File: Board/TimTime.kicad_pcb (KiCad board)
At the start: 4 copper layers, 1.2 x 12 mm, 57 parts, among them IC1 MCP73834-CNI_MF, IC2 LT1761ES5-2.8#TRMPBF, J1 USB4085-GF-A_REVA, J2 SJ1-3523NG, J3 Conn_01x04, J4 Conn_01x06, J5 Conn_01x02, J6 Conn_01x02, U1 STM32L433CCTx, U2 24AA00T_OT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

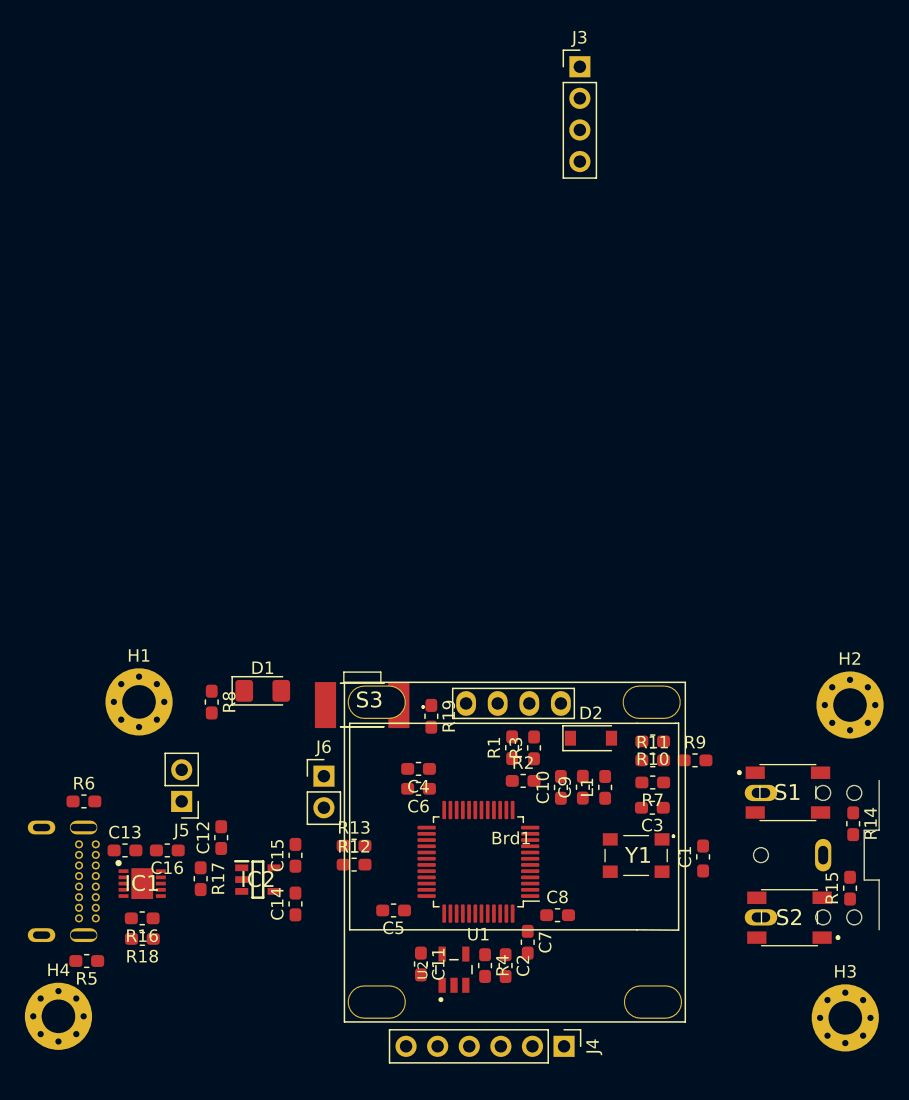
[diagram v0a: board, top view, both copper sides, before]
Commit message: Layout/Routing
Full V01 layout and routing
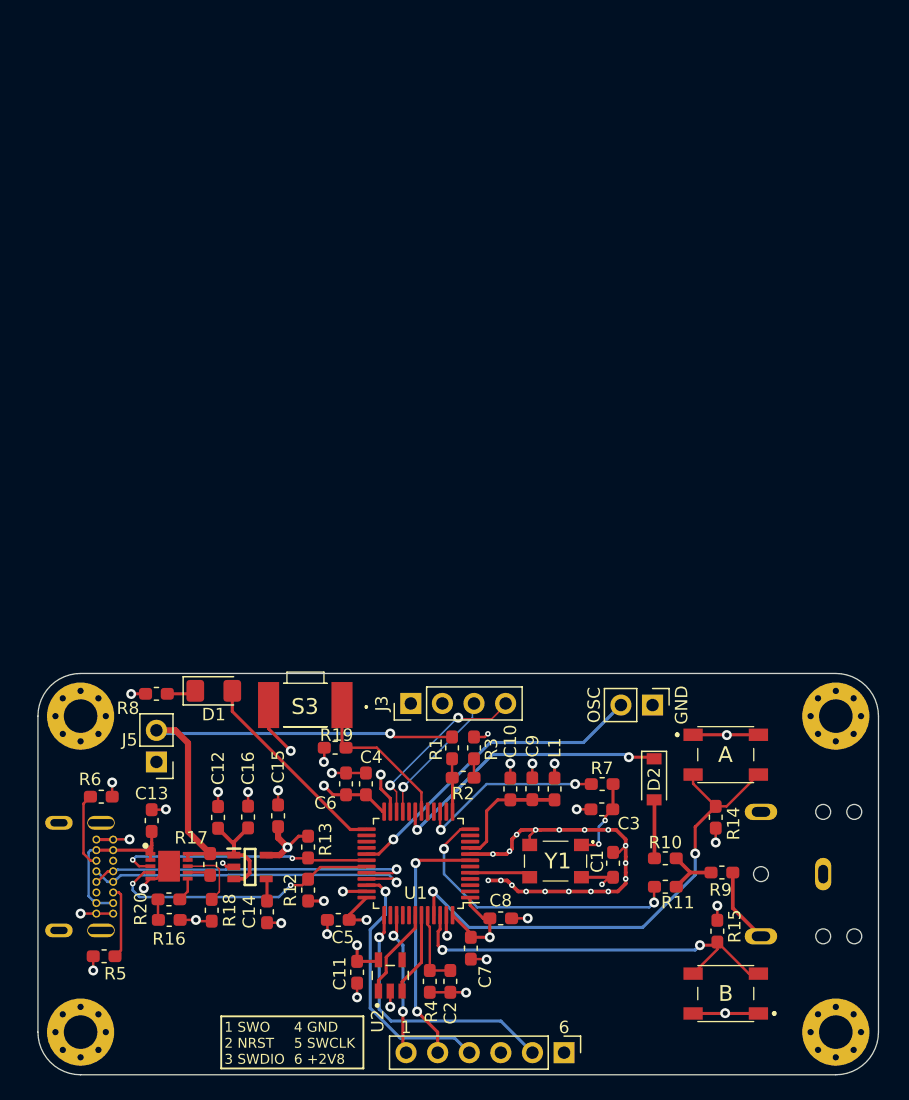
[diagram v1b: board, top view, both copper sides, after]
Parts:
- removed Brd1: SSD1306, SSD1306:128x64OLED
- added G***: LOGO, Slate_Logo:Slate_Logo_01_Back_Silk, F.Cu at (143.0, 104.4)
- added R20: 2K, Resistor_SMD:R_0603_1608Metric_Pad1.05x0.95mm_HandSolder, F.Cu at (120.9, 109.0)
- moved J3 53.0 mm to (140.3, 91.6), turned to 90 degrees
- moved GND 27.0 mm to (159.8, 91.7), turned to 270 degrees
- moved R15 11.2 mm to (165.0, 109.9)
- moved R14 11.1 mm to (164.8, 100.7)
- moved R11 10.2 mm to (160.8, 106.3)
- moved R10 9.45 mm to (160.8, 104.0)
- moved R9 9.27 mm to (165.3, 105.2)
- moved R19 8.14 mm to (134.3, 95.1), turned to 180 degrees
- moved B 7.96 mm to (165.7, 114.9)
- moved C1 7.26 mm to (156.6, 104.4)
- moved C16 7.02 mm to (127.3, 100.7), turned to 90 degrees
- moved Y1 6.49 mm to (152.0, 104.2)
- moved D2 6.06 mm to (159.9, 97.7), turned to 270 degrees
- moved R18 6.03 mm to (124.3, 108.2), turned to 270 degrees
- moved A 5.85 mm to (165.7, 95.7)
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- renumbered S1 to A, S2 to B, J6 to GND
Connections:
- R16 pad 2: GND -> Net-(R16-Pad2)
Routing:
- net GND: track 0.00 -> 79.9 mm, vias 0 -> 48
- net +BATT: track 0.00 -> 50.3 mm, vias 0 -> 1
- net +2V8: track 0.00 -> 49.2 mm, vias 0 -> 11
- net BTN_A: track 0.00 -> 40.2 mm, vias 0 -> 2
- net BTN_B: track 0.00 -> 33.1 mm, vias 0 -> 2
- net USB_D+: track 0.00 -> 27.5 mm, vias 0 -> 1
- net USB_D-: track 0.00 -> 27.1 mm, vias 0 -> 1
- net OSC: track 0.00 -> 25.4 mm, vias 0 -> 1
- net TC_IN: track 0.00 -> 24.4 mm, vias 0 -> 2
- net TC_OUT: track 0.00 -> 23.2 mm, vias 0 -> 2
- net STAT2: track 0.00 -> 22.4 mm, vias 0 -> 2
- net SWCLK: track 0.00 -> 21.5 mm, vias 0 -> 1
- net SWDIO: track 0.00 -> 21.1 mm, vias 0 -> 1
- net STAT1: track 0.00 -> 20.7 mm, vias 0 -> 2
- net NRST: track 0.00 -> 20.5 mm, vias 0 -> 2
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- added copper zone on In2.Cu, net +2V8
- added copper zone on In1.Cu, net GND
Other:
- board size 1.2 x 12 mm -> 67.6 x 32.3 mm
- board text added: "+BATT"
- board text added: "1"
- board text added: "1 SWO 2 NRST 3 SWDIO"
- board text added: "4 GND 5 SWCLK 6 +2V8"
- board text added: "6"
- board text added: "GND"
- board text added: "OSC"

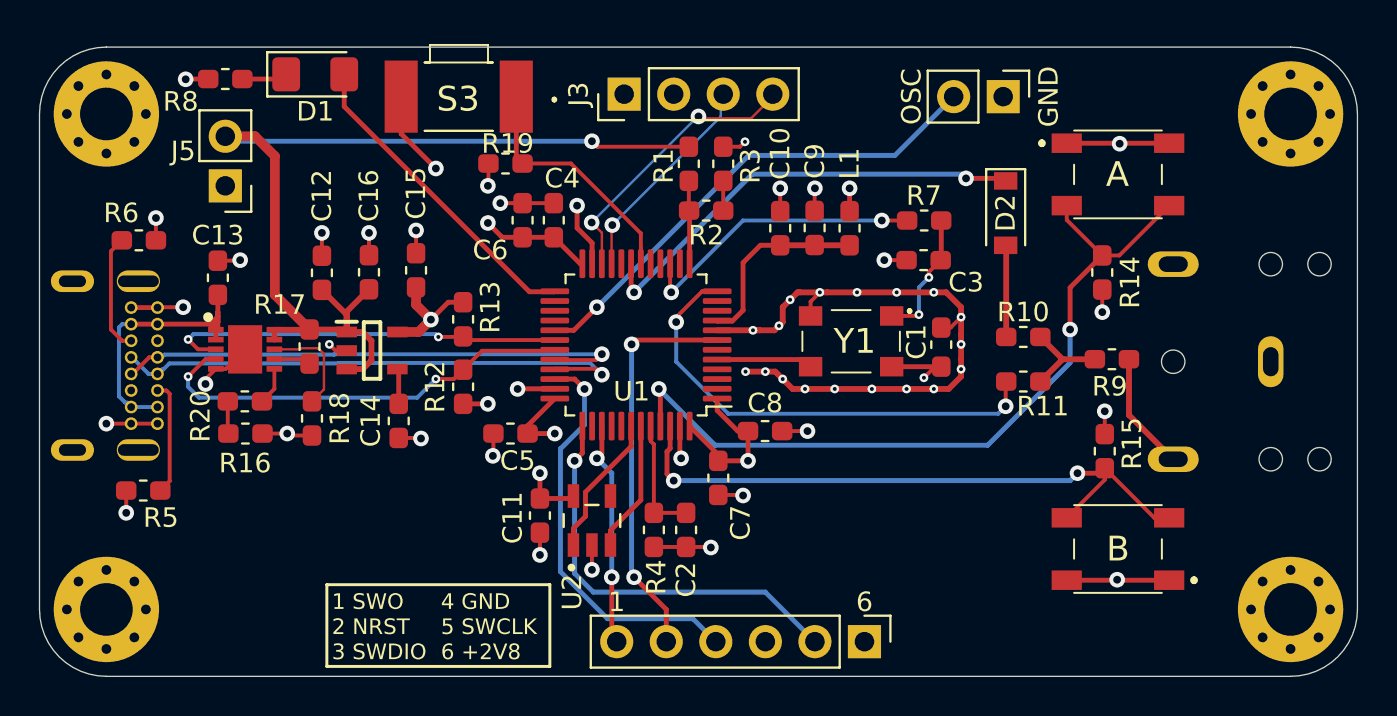
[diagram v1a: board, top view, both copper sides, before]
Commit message: Update layout
Smaller footprint
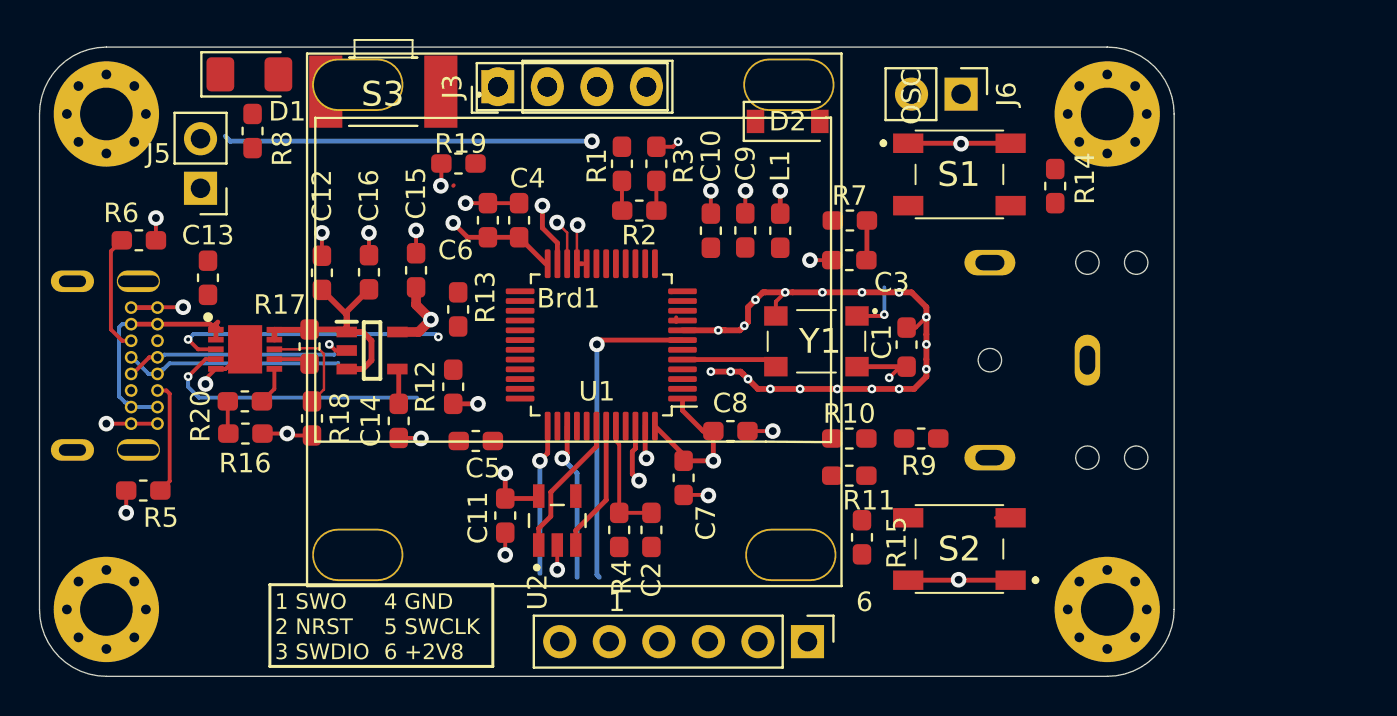
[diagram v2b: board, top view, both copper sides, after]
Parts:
- removed G***: LOGO, Slate_Logo:Slate_Logo_01_Back_Silk
- added Brd1: SSD1306, SSD1306:128x64OLED, F.Cu at (137.5, 101.8)
- moved R15 13.2 mm to (152.5, 114.3), turned to 270 degrees
- moved D2 12.1 mm to (148.7, 93.0), turned to 0 degrees
- moved R9 10.6 mm to (155.6, 109.2)
- moved R10 10.3 mm to (151.9, 109.2)
- moved R11 10.1 mm to (151.9, 111.1)
- moved J2 9.40 mm to (164.1, 105.2)
- moved H2 9.40 mm to (165.1, 92.6)
- moved H3 9.40 mm to (165.1, 118.0)
- moved S1 8.13 mm to (157.5, 95.7)
- moved S2 8.13 mm to (157.5, 114.9)
- moved J3 6.49 mm to (133.9, 91.2)
- moved R14 5.05 mm to (162.4, 96.3), turned to 90 degrees
- moved S3 3.88 mm to (128.0, 91.4)
- moved C3 3.81 mm to (151.9, 100.1)
- moved R7 3.81 mm to (151.9, 98.0)
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- renumbered GND to J6, A to S1, B to S2
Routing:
- net BTN_A: track 40.2 -> 0.00 mm, vias 2 -> 0
- net BTN_B: track 33.1 -> 3.76 mm, vias 2 -> 1
- net OSC: track 25.4 -> 0.00 mm, vias 1 -> 0
- net TC_IN: track 24.4 -> 0.08 mm, vias 2 -> 0
- net TC_OUT: track 23.2 -> 0.00 mm, vias 2 -> 0
- net SWDIO: track 21.1 -> 0.00 mm, vias 1 -> 0
- net +BATT: track 50.3 -> 32.6 mm
- net LED_STATUS: track 16.4 -> 0.00 mm
- net USB_D+: track 27.5 -> 11.2 mm, vias 1 -> 0
- net USB_D-: track 27.1 -> 10.9 mm, vias 1 -> 0
- net TCVC: track 15.1 -> 0.00 mm, vias 2 -> 0
- net SWCLK: track 21.5 -> 7.71 mm
- net BTN_PWR: track 13.4 -> 0.00 mm
- net MON_SDA: track 14.4 -> 2.33 mm, vias 2 -> 1
- net GND: track 79.9 -> 69.3 mm, vias 48 -> 41
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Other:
- board size 67.6 x 32.3 mm -> 58.2 x 32.3 mm

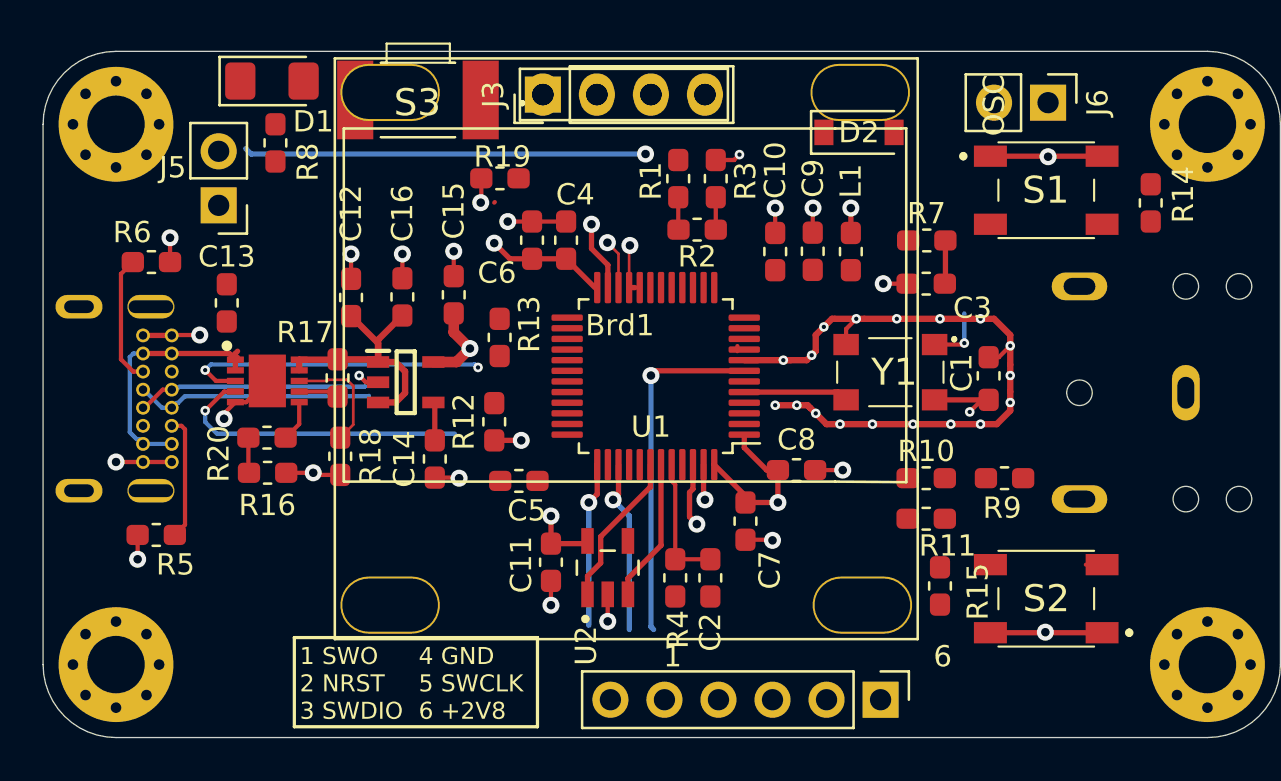
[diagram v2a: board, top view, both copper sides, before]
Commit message: Updated routing
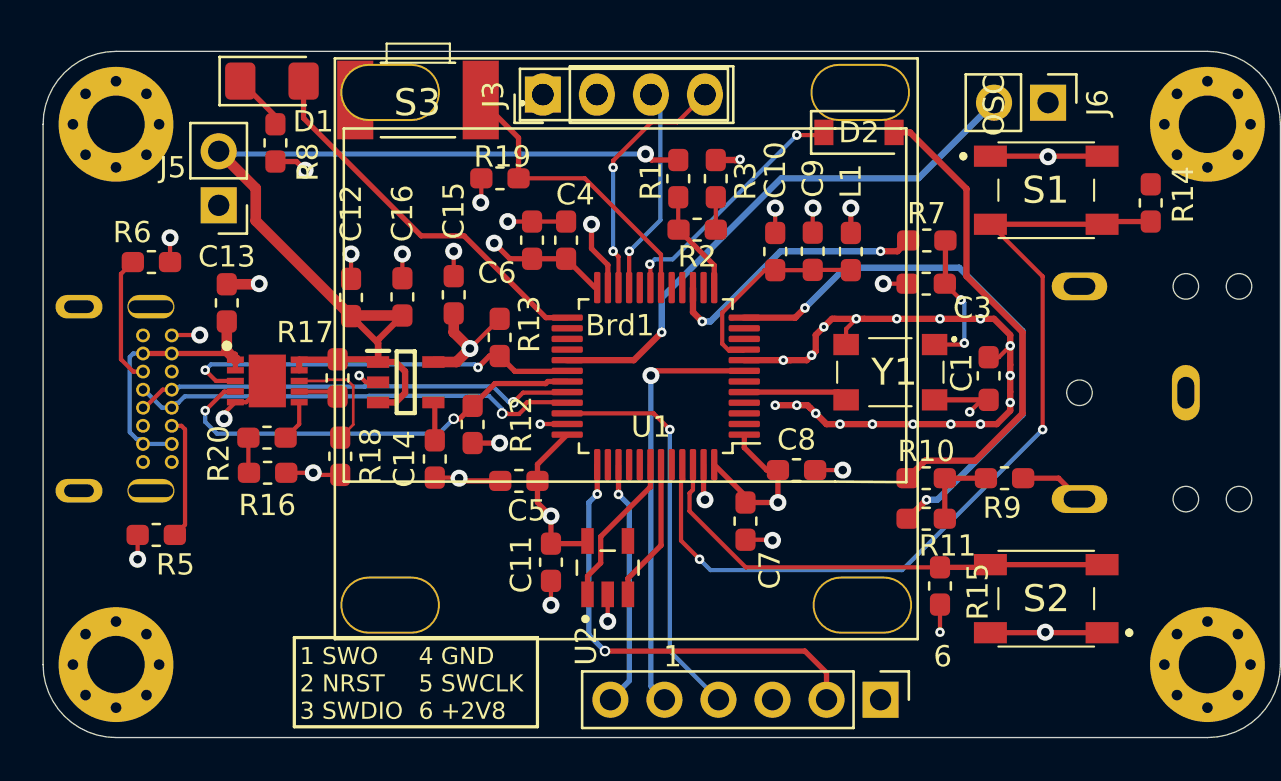
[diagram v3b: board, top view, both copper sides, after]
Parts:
- removed C2: 12uF, Capacitor_SMD:C_0603_1608Metric_Pad1.05x0.95mm_HandSolder
- removed R4: 1M, Resistor_SMD:R_0603_1608Metric_Pad1.05x0.95mm_HandSolder
- moved R12 1.02 mm to (130.6, 106.7)
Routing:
- net BTN_A: track 0.00 -> 41.5 mm, vias 0 -> 2
- net TC_IN: track 0.08 -> 26.7 mm, vias 0 -> 2
- net OSC: track 0.00 -> 26.0 mm, vias 0 -> 1
- net Net-(D2-Pad2): track 0.00 -> 22.8 mm
- net BTN_B: track 3.76 -> 23.6 mm, vias 1 -> 0
- net SWDIO: track 0.00 -> 18.8 mm, vias 0 -> 1
- net LED_STATUS: track 0.00 -> 18.0 mm
- net +BATT: track 32.6 -> 48.2 mm
- net BTN_PWR: track 0.00 -> 14.2 mm
- net SWCLK: track 7.71 -> 21.3 mm, vias 1 -> 2
- net TCVC: track 0.00 -> 13.0 mm, vias 0 -> 2
- net TC_OUT: track 0.00 -> 11.8 mm, vias 0 -> 2
- net USB_D+: track 11.2 -> 21.3 mm, vias 0 -> 1
- net USB_D-: track 10.9 -> 20.9 mm, vias 0 -> 1
- net MON_SDA: track 2.33 -> 11.7 mm, vias 1 -> 2
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
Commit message: V02 routing. VddUSB
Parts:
- removed Brd1: SSD1306, SSD1306:128x64OLED
- added C17: 1.2uF, Capacitor_SMD:C_0603_1608Metric_Pad1.08x0.95mm_HandSolder, F.Cu at (130.2, 112.5)
- added C18: 100nF, Capacitor_SMD:C_0603_1608Metric_Pad1.08x0.95mm_HandSolder, F.Cu at (126.9, 115.1)
- added C2: 1.2uF, Capacitor_SMD:C_0603_1608Metric_Pad1.08x0.95mm_HandSolder, F.Cu at (123.3, 112.1)
- added IC3: LTC1844ES5-3.3#TRPBF, LT1761ES5-2.8#TRMPBF:SOT95P280X100-5N, F.Cu at (126.5, 112.6)
- moved R14 0.38 mm to (162.4, 96.7)
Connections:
- net BOOT0 renamed Net-(U1-Pad44)
- C5 pad 1: +2V8 -> +3V3
- U1 pad 10: Net-(U1-Pad10) -> BTN_PWR
- U1 pad 18: BTN_PWR -> Net-(U1-Pad18)
- U1 pad 36: +2V8 -> +3V3
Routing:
- net Net-(J1-PadP1): track 0.00 -> 15.4 mm
- net GND: track 76.6 -> 89.3 mm, vias 44 -> 50
- net +BATT: track 48.2 -> 60.6 mm
- net +3V3: track 0.00 -> 9.54 mm
- net Net-(C18-Pad2): track 0.00 -> 1.48 mm
- net +2V8: track 45.4 -> 45.6 mm, vias 9 -> 10
- net VAA: track 9.54 -> 9.62 mm, vias 0 -> 2

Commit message: Finalize V02 routing
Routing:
- net BTN_PWR: track 14.2 -> 20.6 mm, vias 0 -> 2

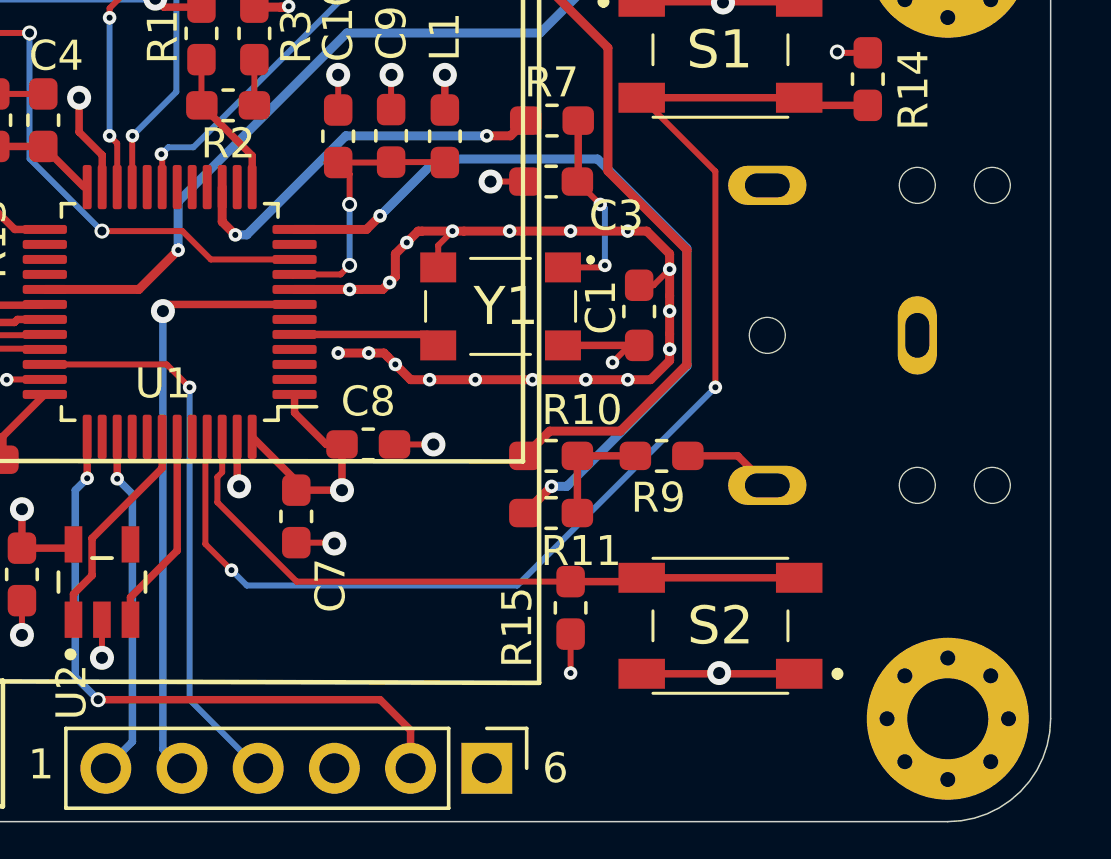
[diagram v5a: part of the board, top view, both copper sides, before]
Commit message: Add additional button, include libraries
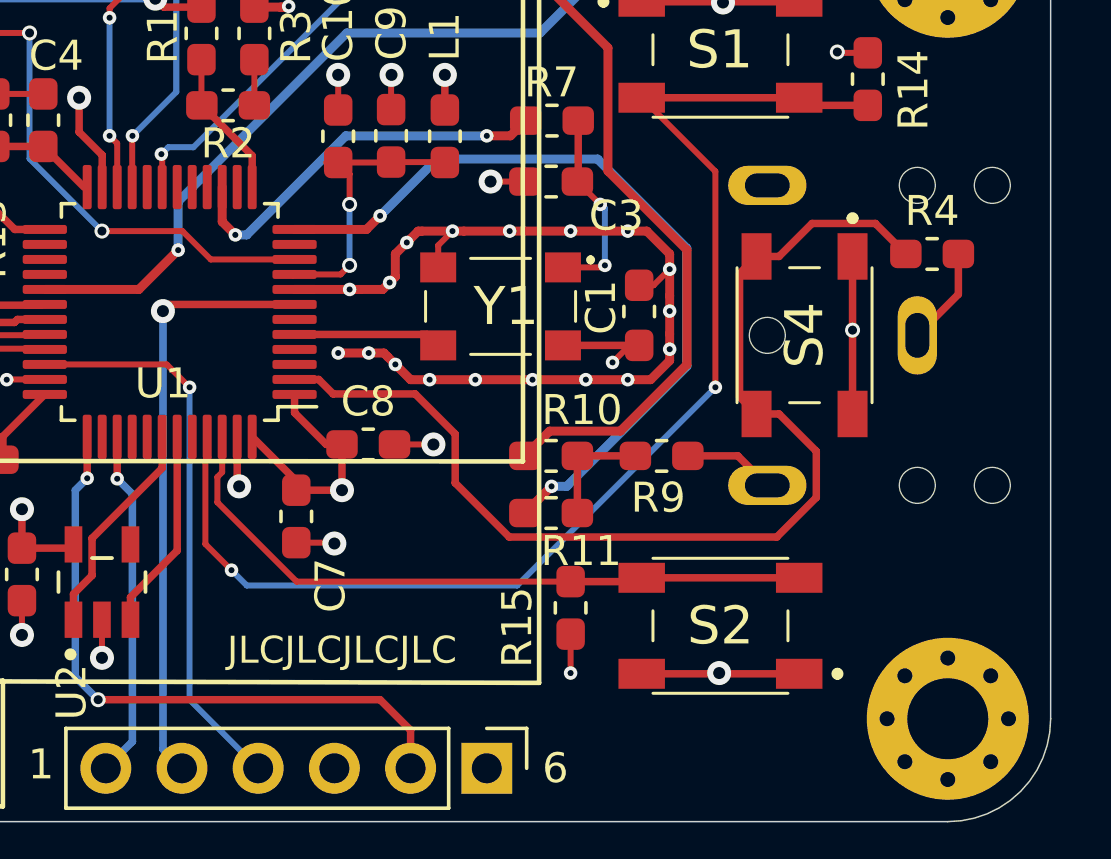
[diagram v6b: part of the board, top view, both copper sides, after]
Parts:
- added R4: 100k, Resistor_SMD:R_0603_1608Metric_Pad1.05x0.95mm_HandSolder, F.Cu at (164.6, 102.5)
- added S4: PTS647SM70SMTR2LFS, PTS647SM70SMTR2LFS:PTS647SM38SMTR2LFS, F.Cu at (160.3, 105.2)
- C15, C17: value 1.2uF -> 12uF
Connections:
- U1 pad 2: Net-(U1-Pad2) -> BTN_C
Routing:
- net BTN_C: track 0.00 -> 36.7 mm
- net +2V8: track 45.6 -> 50.9 mm, vias 10 -> 11
- net GND: track 89.3 -> 92.6 mm
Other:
- board text added: "JLCJLCJLCJLC"
- board text added: "TimTime Lockit Rev. A-001"
